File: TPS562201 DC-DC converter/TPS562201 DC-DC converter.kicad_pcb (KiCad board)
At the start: 2 copper layers, 18.9 x 21.9 mm, 13 parts, among them J1 Conn_01x07_Male, U1 TPS562201

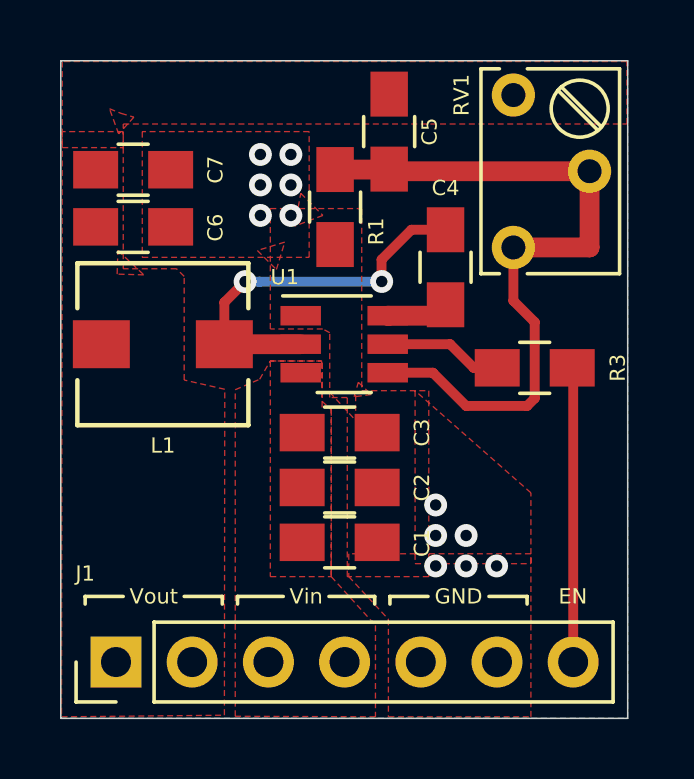
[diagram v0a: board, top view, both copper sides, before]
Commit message: Schematic and layout correction.
Changed how trimmer potentiometer is connected.
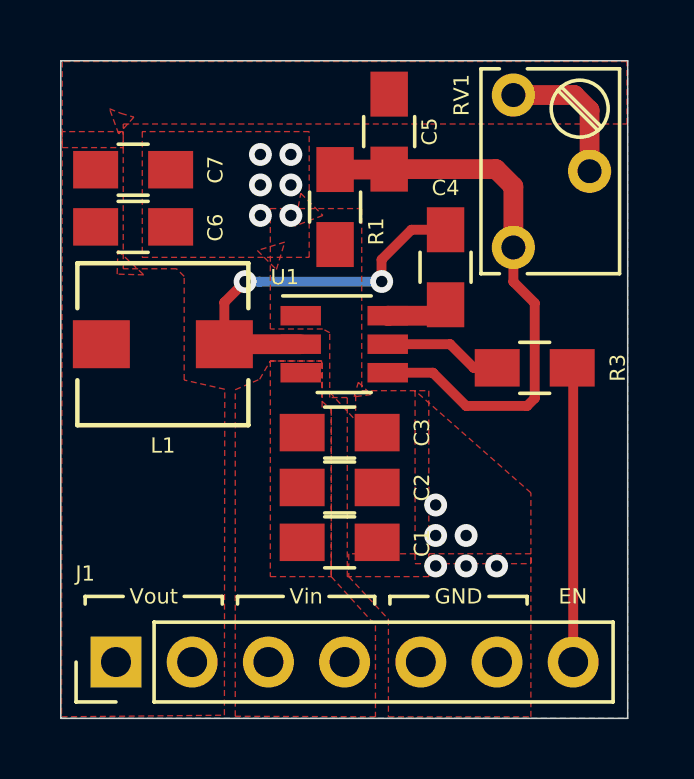
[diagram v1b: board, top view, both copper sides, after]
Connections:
- RV1 pad 2: /VFB -> /VOUT
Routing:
- net /VFB: track 24.4 -> 19.0 mm
- net /VOUT: track 0.00 -> 4.78 mm
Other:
- board text added: "TPS562201 DC-DC converter Bobrowicz, Przemyslaw 6/10/2021 Rev B"
- board text removed: "TPS56201 DC-DC converter Bobrowicz, Przemyslaw 4/14/2021 Rev A"
